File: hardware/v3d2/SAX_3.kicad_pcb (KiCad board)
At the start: 2 copper layers, 86 parts, among them J1 J - 3.3 G, J2 LED strip, J3 SSD1306 G 3.3, J4 Midi M4 M2 M5, J5 Batt, J6 Beak - R BK Y, J7 Conn_01x03_Female, J8 MXP5010, U1 74HC165, U2 74HC165, U3 74HC165, U4 Teensy3.2 - USB ->

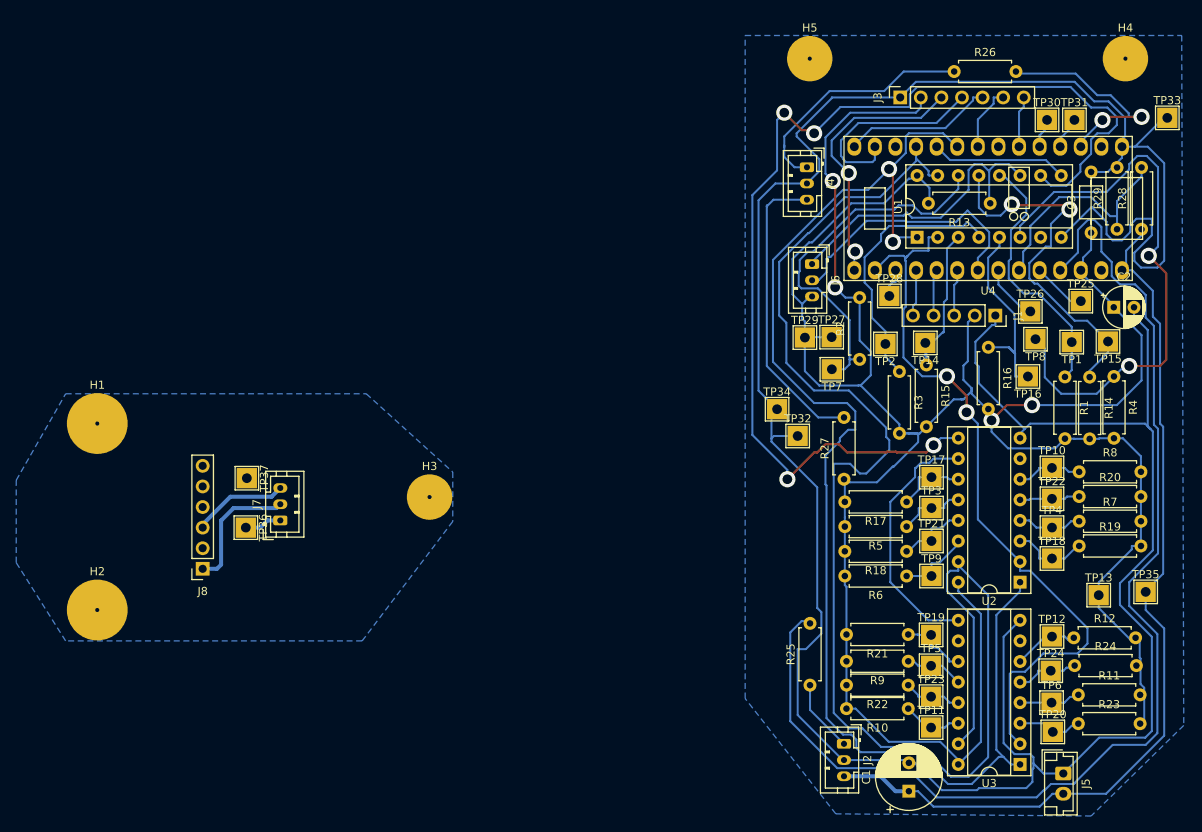
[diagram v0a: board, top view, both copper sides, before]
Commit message: Working PCB, improvments on breath input filtering
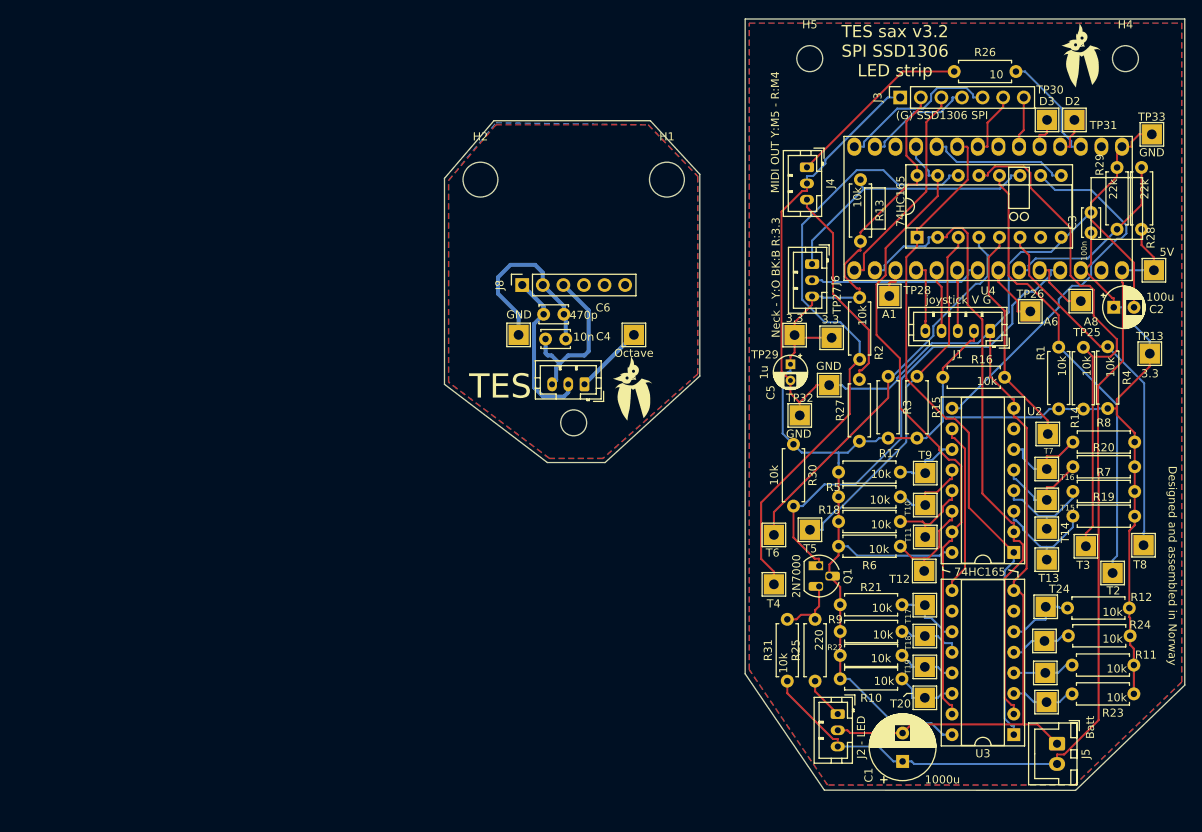
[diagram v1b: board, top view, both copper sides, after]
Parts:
- added C4: 10n, Capacitor_THT:C_Disc_D3.4mm_W2.1mm_P2.50mm, F.Cu at (180.4, 56.0)
- added C5: 1u, Capacitor_THT:CP_Radial_D4.0mm_P2.00mm, F.Cu at (208.2, 59.1)
- added C6: 470p, Capacitor_THT:C_Disc_D3.4mm_W2.1mm_P2.50mm, F.Cu at (180.2, 52.9)
- added G***: LOGO, PCB_symbols:owl_7x10, F.Cu at (188.7, 62.3)
- added G***: LOGO, PCB_symbols:owl_7x10, F.Cu at (244.0, 21.2)
- added G***: LOGO, PCB_symbols:owl_F_50x70, B.Cu at (230.0, 52.4)
- added Q1: 2N7000, Package_TO_SOT_THT:TO-92_HandSolder, F.Cu at (211.7, 84.0)
- added R30: 10k, Resistor_THT:R_Axial_DIN0207_L6.3mm_D2.5mm_P7.62mm_Horizontal, F.Cu at (208.5, 69.0)
- added R31: 10k, Resistor_THT:R_Axial_DIN0207_L6.3mm_D2.5mm_P7.62mm_Horizontal, F.Cu at (207.8, 98.2)
- C1: value 1000u Ch -> 1000u
- C3: value 0.1 ceram -> 100n; footprint Capacitor_THT:C_Axial_L3.8mm_D2.6mm_P7.50mm_Horizontal -> Capacitor_THT:C_Disc_D3.4mm_W2.1mm_P2.50mm
- H1, H2: value MountingHole -> M4; footprint MountingHole:MountingHole_4.3mm_M4_DIN965_Pad -> MountingHole:MountingHole_4.3mm_M4
- H3, H4, H5: value MountingHole -> M3; footprint MountingHole:MountingHole_3.2mm_M3_DIN965_Pad -> MountingHole:MountingHole_3.2mm_M3
- J1: value J - 3.3 G -> joystick V G; footprint Connector_PinSocket_2.54mm:PinSocket_1x05_P2.54mm_Vertical -> Connector_JST:JST_PH_B5B-PH-K_1x05_P2.00mm_Vertical
- J2 - LED: renamed from J2
- J3: value SSD1306 G 3.3 -> (G) SSD1306 SPI
- J4: value Midi M4 M2 M5 -> MIDI OUT Y:M5 - R:M4
- J5: footprint Connector_JST:JST_EH_B2B-EH-A_1x02_P2.50mm_Vertical -> Connector_JST:JST_XH_B2B-XH-A_1x02_P2.50mm_Vertical
- J6: value Beak - R BK Y -> Neck - Y:O BK:B R:3.3
- U4: value Teensy3.2 - USB -> -> Teensy3.2_breadboard_friendly
- moved H1 76.4 mm to (192.9, 36.3)
- moved H2 71.1 mm to (169.9, 36.3)
- moved TP36 53.5 mm to (188.8, 55.5), turned to 0 degrees
- moved J8 52.7 mm to (175.1, 49.3), turned to 90 degrees
- moved J7 41.1 mm to (182.7, 61.6), turned to 180 degrees
- moved TP35 39.7 mm to (253.0, 47.5)
- moved TP37 37.9 mm to (174.6, 55.5), turned to 0 degrees
- moved TP13 30.5 mm to (252.5, 57.8)
- moved TP1 28.9 mm to (247.9, 84.8)
- moved TP8 28.7 mm to (251.7, 81.4)
- moved TP7 27.5 mm to (206.1, 86.2)
- moved TP2 27.3 mm to (206.1, 80.1)
- moved TP14 27.1 mm to (210.6, 79.5)
- moved TP15 25.4 mm to (244.6, 81.5)
- moved H3 20.0 mm to (181.4, 66.3)
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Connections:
- J8 pad 4: Net-(J8-Pad4) -> unconnected-(J8-Pad4)
- J8 pad 5: Net-(J8-Pad5) -> unconnected-(J8-Pad5)
- J8 pad 6: Net-(J8-Pad6) -> unconnected-(J8-Pad6)
- R25 pad 2: Net-(R25-Pad2) -> Net-(Q1-Pad3)
- U1 pad 7: Net-(U1-Pad7) -> unconnected-(U1-Pad7)
- U2 pad 7: Net-(U2-Pad7) -> unconnected-(U2-Pad7)
- U3 pad 10: Net-(U3-Pad10) -> unconnected-(U3-Pad10)
- U3 pad 7: Net-(U3-Pad7) -> unconnected-(U3-Pad7)
- U4 pad 12: Net-(U4-Pad12) -> unconnected-(U4-Pad12)
- U4 pad 2: Net-(U4-Pad2) -> unconnected-(U4-Pad2)
- U4 pad 30: Net-(R25-Pad2) -> Net-(Q1-Pad1)
- U4 pad 32: Net-(U4-Pad32) -> unconnected-(U4-Pad32)
- U4 pad 7: Net-(U4-Pad7) -> unconnected-(U4-Pad7)
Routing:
- net GND: track 359.1 -> 207.4 mm
- net Net-(R25-Pad2): track 145.5 -> 0.00 mm
- net /SR_CLK_INH: track 172.6 -> 81.4 mm
- net Net-(U1-Pad10): track 136.3 -> 46.2 mm, vias 4 -> 0
- net +3V3: track 323.8 -> 242.9 mm, vias 4 -> 0
- net /SR_SH: track 161.5 -> 84.3 mm, vias 2 -> 0
- net Net-(Q1-Pad1): track 0.00 -> 59.9 mm
- net Net-(R2-Pad1): track 46.1 -> 77.5 mm
- net Net-(R4-Pad1): track 70.8 -> 44.9 mm, vias 2 -> 0
- net Net-(R15-Pad1): track 20.3 -> 44.9 mm
- net Net-(J8-Pad2): track 0.00 -> 24.1 mm
- net Net-(R1-Pad1): track 32.0 -> 56.1 mm
- net Net-(R14-Pad1): track 45.9 -> 62.9 mm, vias 2 -> 0
- net Net-(R3-Pad1): track 33.3 -> 48.7 mm
- net Net-(R26-Pad2): track 27.4 -> 13.9 mm, vias 2 -> 0
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- added copper zone on F.Cu, net GND
- added copper zone on F.Cu, net Net-(J8-Pad2)
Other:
- board outline added: 91.3 x 95.1 mm
- rule pad_to_mask_clearance: 0.051 -> 0
- board text added: "Designed and assembled in Norway"
- board text added: "TES"
- board text added: "TES sax v3.2 SPI SSD1306 LED strip"
- board text removed: "TES sax v3.1 SPI SSD1306 LED strip"
